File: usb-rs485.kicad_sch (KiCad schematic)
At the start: 0 parts

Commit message: routed, thru holes. ready to order i think
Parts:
- added J2, J3: ~, robot-cortex:ThruHoleBreadboardX4, symbol usb-rs485:ThruHoleX4
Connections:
- net 3V3: now also J3.1
- net GND: now also J2.4, J3.4
- net RX: now also J3.2
- net TX: now also J3.3
- net VUSB: now also J2.1
- new net RS485 Transceiver/RS485-A: J2.2
- new net RS485 Transceiver/RS485-B: J2.3
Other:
- sheet RS485 Transceiver ports: added RS485-A, RS485-B; removed none
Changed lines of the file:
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@@
 (kicad_sch (version 20230121) (generator eeschema)
   (paper "A3")
+  (wire (pts (xy 328.93 173.99) (xy 328.93 174.625))
+    (stroke (width 0) (type default))
+  )
+  (wire (pts (xy 328.93 154.94) (xy 328.93 155.575))
+    (stroke (width 0) (type default))
+  )
   (wire (pts (xy 295.91 144.78) (xy 299.085 144.78))
     (stroke (width 0) (type default))
   )
+  (wire (pts (xy 328.93 166.37) (xy 329.565 166.37))
+    (stroke (width 0) (type default))
+  )
+  (wire (pts (xy 328.93 173.99) (xy 329.565 173.99))
+    (stroke (width 0) (type default))
+  )
+  (wire (pts (xy 328.93 165.735) (xy 328.93 166.37))
+    (stroke (width 0) (type default))
+  )
   (wire (pts (xy 279.4 152.4) (xy 299.085 152.4))
     (stroke (width 0) (type default))
@@
     (stroke (width 0) (type default))
   )
+  (wire (pts (xy 322.58 149.86) (xy 329.565 149.86))
+    (stroke (width 0) (type default))
+  )
+  (wire (pts (xy 328.93 147.32) (xy 329.565 147.32))
+    (stroke (width 0) (type default))
+  )
   (wire (pts (xy 295.91 144.78) (xy 295.91 141.605))
     (stroke (width 0) (type default))
@@
     (stroke (width 0) (type default))
   )
+  (wire (pts (xy 322.58 152.4) (xy 329.565 152.4))
+    (stroke (width 0) (type default))
+  )
   (wire (pts (xy 279.4 149.86) (xy 299.085 149.86))
     (stroke (width 0) (type default))
   )
+  (wire (pts (xy 328.93 168.91) (xy 329.565 168.91))
+    (stroke (width 0) (type default))
+  )
+  (wire (pts (xy 328.93 171.45) (xy 329.565 171.45))
+    (stroke (width 0) (type default))
+  )
   (wire (pts (xy 297.18 157.48) (xy 297.18 158.75))
     (stroke (width 0) (type default))
@@
     (stroke (width 0) (type default))
   )
+  (wire (pts (xy 328.93 146.685) (xy 328.93 147.32))
+    (stroke (width 0) (type default))
+  )
+  (wire (pts (xy 328.93 154.94) (xy 329.565 154.94))
+    (stroke (width 0) (type default))
+  )
   (label "VUSB" (at 254.635 142.875 180) (fields_autoplaced)
+    (effects (font (size 1.27 1.27)) (justify right bottom))
+  )
+  (label "TX" (at 328.93 171.45 180) (fields_autoplaced)
     (effects (font (size 1.27 1.27)) (justify right bottom))
   )
@@
     (effects (font (size 1.27 1.27)) (justify right bottom))
   )
+  (label "RX" (at 328.93 168.91 180) (fields_autoplaced)
+    (effects (font (size 1.27 1.27)) (justify right bottom))
+  )
   (label "3V3" (at 293.37 145.415 180) (fields_autoplaced)
     (effects (font (size 1.27 1.27)) (justify right bottom))
@@
   (label "RX" (at 287.02 149.86 0) (fields_autoplaced)
     (effects (font (size 1.27 1.27)) (justify left bottom))
+  )
+  (label "VUSB" (at 328.93 146.685 180) (fields_autoplaced)
+    (effects (font (size 1.27 1.27)) (justify right bottom))
+  )
+  (label "3V3" (at 328.93 165.735 180) (fields_autoplaced)
+    (effects (font (size 1.27 1.27)) (justify right bottom))
   )
   (symbol (lib_id "power:GND") (at 297.18 158.75 0) (unit 1)
@@
     )
   )
-  (sheet (at 299.085 142.875) (size 12.7 16.51)
+  (symbol (lib_id "power:GND") (at 328.93 155.575 0) (unit 1)
+    (in_bom yes) (on_board yes) (dnp no)
+    (property "Reference" "#PWR011" (at 328.93 161.925 0)
+      (effects (font (size 1.27 1.27)) hide)
+    )
+    (property "Value" "GND" (at 328.93 159.385 0)
+      (effects (font (size 1.27 1.27)))
+    )
+    (property "Footprint" "" (at 328.93 155.575 0)
+      (effects (font (size 1.27 1.27)) hide)
+    )
+    (property "Datasheet" "" (at 328.93 155.575 0)
+      (effects (font (size 1.27 1.27)) hide)
+    )
+    (pin "1")
+    (instances
+      (project "usb-rs485"
+        (path "/19e4cb9f-d0a4-4ce0-8aa4-5fe95563dc37"
+          (reference "#PWR011") (unit 1)
+        )
+      )
+    )
+  )
+  (symbol (lib_id "usb-rs485:ThruHoleX4") (at 332.105 170.18 0) (mirror y) (unit 1)
+    (in_bom no) (on_board yes) (dnp no) (fields_autoplaced)
+    (property "Reference" "J3" (at 336.55 170.18 0)
+      (effects (font (size 1.27 1.27)) (justify right))
+    )
+    (property "Value" "~" (at 330.835 168.91 0)
+      (effects (font (size 1.27 1.27)))
+    )
+    (property "Footprint" "robot-cortex:ThruHoleBreadboardX4" (at 330.835 168.91 0)
+      (effects (font (size 1.27 1.27)) hide)
+    )
+    (property "Datasheet" "" (at 330.835 168.91 0)
+      (effects (font (size 1.27 1.27)) hide)
+    )
+    (pin "3")
+    (pin "4")
+    (pin "2")
+    (pin "1")
+    (instances
+      (project "usb-rs485"
+        (path "/19e4cb9f-d0a4-4ce0-8aa4-5fe95563dc37"
+          (reference "J3") (unit 1)
+        )
+      )
+    )
+  )
+  (symbol (lib_id "usb-rs485:ThruHoleX4") (at 332.105 151.13 0) (mirror y) (unit 1)
+    (in_bom no) (on_board yes) (dnp no) (fields_autoplaced)
+    (property "Reference" "J2" (at 336.55 151.13 0)
+      (effects (font (size 1.27 1.27)) (justify right))
+    )
+    (property "Value" "~" (at 330.835 149.86 0)
+      (effects (font (size 1.27 1.27)))
+    )
+    (property "Footprint" "robot-cortex:ThruHoleBreadboardX4" (at 330.835 149.86 0)
+      (effects (font (size 1.27 1.27)) hide)
+    )
+    (property "Datasheet" "" (at 330.835 149.86 0)
+      (effects (font (size 1.27 1.27)) hide)
+    )
+    (pin "3")
+    (pin "4")
+    (pin "2")
+    (pin "1")
+    (instances
+      (project "usb-rs485"
+        (path "/19e4cb9f-d0a4-4ce0-8aa4-5fe95563dc37"
+          (reference "J2") (unit 1)
+        )
+      )
+    )
+  )
+  (symbol (lib_id "power:GND") (at 328.93 174.625 0) (unit 1)
+    (in_bom yes) (on_board yes) (dnp no)
+    (property "Reference" "#PWR012" (at 328.93 180.975 0)
+      (effects (font (size 1.27 1.27)) hide)
+    )
+    (property "Value" "GND" (at 328.93 178.435 0)
+      (effects (font (size 1.27 1.27)))
+    )
+    (property "Footprint" "" (at 328.93 174.625 0)
+      (effects (font (size 1.27 1.27)) hide)
+    )
+    (property "Datasheet" "" (at 328.93 174.625 0)
+      (effects (font (size 1.27 1.27)) hide)
+    )
+    (pin "1")
+    (instances
+      (project "usb-rs485"
+        (path "/19e4cb9f-d0a4-4ce0-8aa4-5fe95563dc37"
+          (reference "#PWR012") (unit 1)
+        )
+      )
+    )
+  )
+  (sheet (at 299.085 142.875) (size 23.495 16.51)
     (stroke (width 0.1524) (type solid))
     (fill (color 0 0 0 0.0000))
@@
       (effects (font (size 1.27 1.27)) (justify left))
     )
-    (instances
+    (pin "RS485-B" input (at 322.58 152.4 0)
+      (effects (font (size 1.27 1.27)) (justify right))
+    )
+    (pin "RS485-A" input (at 322.58 149.86 0)
+      (effects (font (size 1.27 1.27)) (justify right))
+    )
+    (instances

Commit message: rename library to be for this
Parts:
- J2, J3: footprint robot-cortex:ThruHoleBreadboardX4 -> usb-rs485:ThruHoleBreadboardX4
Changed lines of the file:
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@@
       (effects (font (size 1.27 1.27)))
     )
-    (property "Footprint" "robot-cortex:ThruHoleBreadboardX4" (at 330.835 168.91 0)
+    (property "Footprint" "usb-rs485:ThruHoleBreadboardX4" (at 330.835 168.91 0)
       (effects (font (size 1.27 1.27)) hide)
     )
@@
       (effects (font (size 1.27 1.27)))
     )
-    (property "Footprint" "robot-cortex:ThruHoleBreadboardX4" (at 330.835 149.86 0)
+    (property "Footprint" "usb-rs485:ThruHoleBreadboardX4" (at 330.835 149.86 0)
       (effects (font (size 1.27 1.27)) hide)
     )

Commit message: starting to add power
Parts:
- added R4: 470k, usb-rs485:R_0402_1005Metric, symbol usb-rs485:Resistor
- added R5: 150k, usb-rs485:R_0402_1005Metric, symbol usb-rs485:Resistor
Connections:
- new net PSU_TPS63070RNMR/FB: R4.2, R5.1
- new net PSU_TPS63070RNMR/FB_GND: R5.2
- new net PSU_TPS63070RNMR/FB_VOUT: R4.1
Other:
- added sheet PSU_TPS63070RNMR (PSU_TPS63070RNMR.kicad_sch)
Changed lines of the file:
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@@
 (kicad_sch (version 20230121) (generator eeschema)
   (paper "A3")
+  (junction (at 302.26 202.565) (diameter 0) (color 0 0 0 0)
+  )
+  (junction (at 285.115 180.975) (diameter 0) (color 0 0 0 0)
+  )
   (wire (pts (xy 328.93 173.99) (xy 328.93 174.625))
     (stroke (width 0) (type default))
   )
+  (wire (pts (xy 285.115 178.435) (xy 285.115 180.975))
+    (stroke (width 0) (type default))
+  )
   (wire (pts (xy 328.93 154.94) (xy 328.93 155.575))
     (stroke (width 0) (type default))
   )
+  (wire (pts (xy 302.26 202.565) (xy 300.355 202.565))
+    (stroke (width 0) (type default))
+  )
+  (wire (pts (xy 300.355 181.61) (xy 301.625 181.61))
+    (stroke (width 0) (type default))
+  )
   (wire (pts (xy 295.91 144.78) (xy 299.085 144.78))
     (stroke (width 0) (type default))
@@
     (stroke (width 0) (type default))
   )
+  (wire (pts (xy 302.26 213.995) (xy 300.355 213.995))
+    (stroke (width 0) (type default))
+  )
   (wire (pts (xy 279.4 152.4) (xy 299.085 152.4))
     (stroke (width 0) (type default))
@@
     (stroke (width 0) (type default))
   )
+  (wire (pts (xy 302.26 192.405) (xy 302.26 193.04))
+    (stroke (width 0) (type default))
+  )
   (wire (pts (xy 328.93 147.32) (xy 329.565 147.32))
     (stroke (width 0) (type default))
   )
+  (wire (pts (xy 285.115 186.69) (xy 285.115 186.055))
+    (stroke (width 0) (type default))
+  )
   (wire (pts (xy 295.91 144.78) (xy 295.91 141.605))
     (stroke (width 0) (type default))
@@
     (stroke (width 0) (type default))
   )
+  (wire (pts (xy 300.355 192.405) (xy 302.26 192.405))
+    (stroke (width 0) (type default))
+  )
   (wire (pts (xy 257.81 142.875) (xy 254.635 142.875))
     (stroke (width 0) (type default))
@@
     (stroke (width 0) (type default))
   )
+  (wire (pts (xy 302.26 212.09) (xy 302.26 213.995))
+    (stroke (width 0) (type default))
+  )
   (wire (pts (xy 297.18 157.48) (xy 297.18 158.75))
     (stroke (width 0) (type default))
@@
     (stroke (width 0) (type default))
   )
+  (wire (pts (xy 283.21 178.435) (xy 285.115 178.435))
+    (stroke (width 0) (type default))
+  )
   (wire (pts (xy 254.635 160.655) (xy 254.635 163.195))
     (stroke (width 0) (type default))
   )
+  (wire (pts (xy 285.115 180.975) (xy 287.02 180.975))
+    (stroke (width 0) (type default))
+  )
   (wire (pts (xy 257.81 160.655) (xy 254.635 160.655))
     (stroke (width 0) (type default))
   )
+  (wire (pts (xy 302.26 200.66) (xy 302.26 202.565))
+    (stroke (width 0) (type default))
+  )
+  (wire (pts (xy 302.26 202.565) (xy 302.26 204.47))
+    (stroke (width 0) (type default))
+  )
   (wire (pts (xy 293.37 147.32) (xy 293.37 145.415))
     (stroke (width 0) (type default))
   )
+  (wire (pts (xy 285.115 186.055) (xy 287.02 186.055))
+    (stroke (width 0) (type default))
+  )
   (wire (pts (xy 328.93 146.685) (xy 328.93 147.32))
     (stroke (width 0) (type default))
@@
     (stroke (width 0) (type default))
   )
+  (wire (pts (xy 282.575 180.975) (xy 285.115 180.975))
+    (stroke (width 0) (type default))
+  )
+  (label "V_GATEDRIVE" (at 283.21 178.435 180) (fields_autoplaced)
+    (effects (font (size 1.27 1.27)) (justify right bottom))
+  )
   (label "VUSB" (at 254.635 142.875 180) (fields_autoplaced)
     (effects (font (size 1.27 1.27)) (justify right bottom))
   )
   (label "TX" (at 328.93 171.45 180) (fields_autoplaced)
+    (effects (font (size 1.27 1.27)) (justify right bottom))
+  )
+  (label "V_LOGIC" (at 282.575 180.975 180) (fields_autoplaced)
     (effects (font (size 1.27 1.27)) (justify right bottom))
   )
@@
         (path "/19e4cb9f-d0a4-4ce0-8aa4-5fe95563dc37"
           (reference "#PWR073") (unit 1)
+        )
+      )
+    )
+  )
+  (symbol (lib_id "power:GND") (at 285.115 186.69 0) (mirror y) (unit 1)
+    (in_bom yes) (on_board yes) (dnp no) (fields_autoplaced)
+    (property "Reference" "#PWR013" (at 285.115 193.04 0)
+      (effects (font (size 1.27 1.27)) hide)
+    )
+    (property "Value" "GND" (at 285.115 191.77 0)
+      (effects (font (size 1.27 1.27)))
+    )
+    (property "Footprint" "" (at 285.115 186.69 0)
+      (effects (font (size 1.27 1.27)) hide)
+    )
+    (property "Datasheet" "" (at 285.115 186.69 0)
+      (effects (font (size 1.27 1.27)) hide)
+    )
+    (pin "1")
+    (instances
+      (project "usb-rs485"
+        (path "/19e4cb9f-d0a4-4ce0-8aa4-5fe95563dc37"
+          (reference "#PWR013") (unit 1)
+        )
+      )
+    )
+  )
+  (symbol (lib_id "usb-rs485:Resistor") (at 302.26 196.85 0) (unit 1)
+    (in_bom yes) (on_board yes) (dnp no)
+    (property "Reference" "R4" (at 303.53 197.485 0)
+      (effects (font (size 1.27 1.27)) (justify left))
+    )
+    (property "Value" "470k" (at 306.07 199.39 0)
+      (effects (font (size 1.27 1.27)))
+    )
+    (property "Footprint" "usb-rs485:R_0402_1005Metric" (at 297.18 184.15 0)
+      (effects (font (size 1.27 1.27)) hide)
+    )
+    (property "Datasheet" "~" (at 302.26 196.85 0)
+      (effects (font (size 1.27 1.27)) hide)
+    )
+    (pin "1")
+    (pin "2")
+    (instances
+      (project "usb-rs485"
+        (path "/19e4cb9f-d0a4-4ce0-8aa4-5fe95563dc37"
+          (reference "R4") (unit 1)
         )
       )
@@
       )
     )
+  )
+  (symbol (lib_id "power:+3V3") (at 301.625 181.61 0) (mirror y) (unit 1)
+    (in_bom yes) (on_board yes) (dnp no)
+    (property "Reference" "#PWR014" (at 301.625 185.42 0)
+      (effects (font (size 1.27 1.27)) hide)
+    )
+    (property "Value" "+3V3" (at 305.435 180.34 0)
+      (effects (font (size 1.27 1.27)))
+    )
+    (property "Footprint" "" (at 301.625 181.61 0)
+      (effects (font (size 1.27 1.27)) hide)
+    )
+    (property "Datasheet" "" (at 301.625 181.61 0)
+      (effects (font (size 1.27 1.27)) hide)
+    )
+    (pin "1")
+    (instances
+      (project "usb-rs485"
+        (path "/19e4cb9f-d0a4-4ce0-8aa4-5fe95563dc37"
+          (reference "#PWR014") (unit 1)
+        )
+      )
+    )
+  )
+  (symbol (lib_id "usb-rs485:Resistor") (at 302.26 208.28 0) (unit 1)
+    (in_bom yes) (on_board yes) (dnp no)
+    (property "Reference" "R5" (at 303.53 208.915 0)
+      (effects (font (size 1.27 1.27)) (justify left))
+    )
+    (property "Value" "150k" (at 306.07 210.82 0)
+      (effects (font (size 1.27 1.27)))
+    )
+    (property "Footprint" "usb-rs485:R_0402_1005Metric" (at 297.18 195.58 0)
+      (effects (font (size 1.27 1.27)) hide)
+    )
+    (property "Datasheet" "~" (at 302.26 208.28 0)
+      (effects (font (size 1.27 1.27)) hide)
+    )
+    (pin "1")
+    (pin "2")
+    (instances
+      (project "usb-rs485"
+        (path "/19e4cb9f-d0a4-4ce0-8aa4-5fe95563dc37"
+          (reference "R5") (unit 1)
+        )
+      )
+    )
+  )
+  (sheet (at 287.02 179.705) (size 13.335 35.56)
+    (stroke (width 0.1524) (type solid))
+    (fill (color 0 0 0 0.0000))
+    (property "Sheetname" "PSU_TPS63070RNMR" (at 286.385 177.8 0)
+      (effects (font (size 1.27 1.27)) (justify left bottom))
+    )
+    (property "Sheetfile" "PSU_TPS63070RNMR.kicad_sch" (at 287.02 216.535 0)
+      (effects (font (size 1.27 1.27)) (justify left top))
+    )
+    (pin "VOUT" input (at 300.355 181.61 0)
+      (effects (font (size 1.27 1.27)) (justify right))
+    )
+    (pin "GND" input (at 287.02 186.055 180)
+      (effects (font (size 1.27 1.27)) (justify left))
+    )
+    (pin "VIN" input (at 287.02 180.975 180)
+      (effects (font (size 1.27 1.27)) (justify left))
+    )
+    (pin "FB_VOUT" input (at 300.355 192.405 0)
+      (effects (font (size 1.27 1.27)) (justify right))
+    )
+    (pin "FB" input (at 300.355 202.565 0)
+      (effects (font (size 1.27 1.27)) (justify right))
+    )
+    (pin "FB_GND" input (at 300.355 213.995 0)
+      (effects (font (size 1.27 1.27)) (justify right))
+    )
+    (instances
+      (project "foc-pcb"
+        (path "/2b52ab19-a93e-4439-8602-a1380e4825c0" (page "5"))
+      )
+      (project "usb-rs485"
+        (path "/19e4cb9f-d0a4-4ce0-8aa4-5fe95563dc37" (page "3"))
+      )
+    )

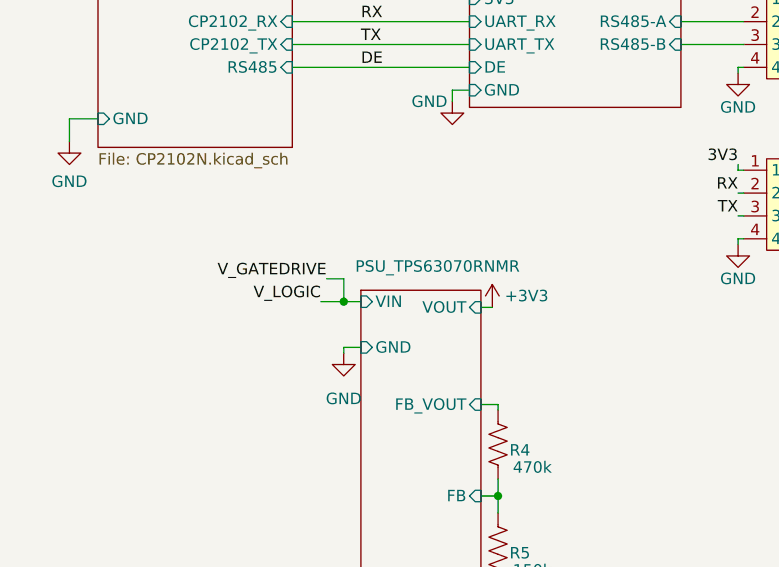
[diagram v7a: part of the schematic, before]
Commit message: wiring in boost to 6V
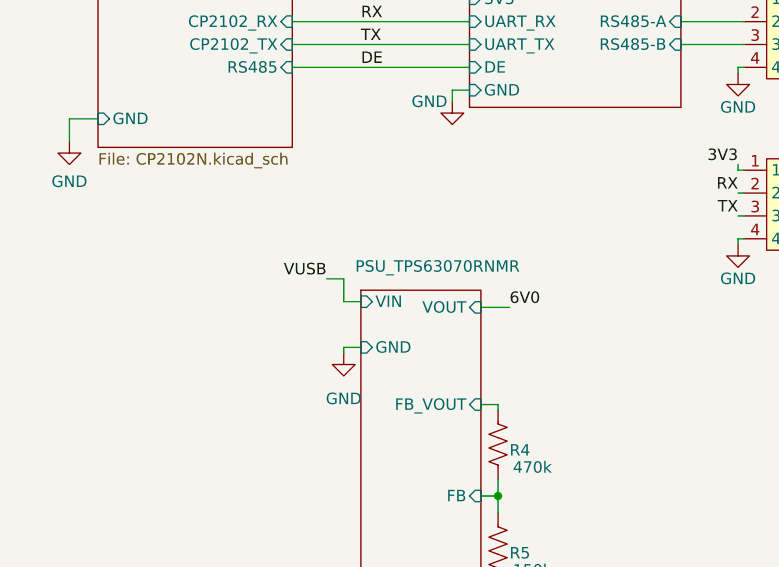
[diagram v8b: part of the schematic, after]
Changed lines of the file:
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@@
   (junction (at 302.26 202.565) (diameter 0) (color 0 0 0 0)
   )
-  (junction (at 285.115 180.975) (diameter 0) (color 0 0 0 0)
-  )
   (wire (pts (xy 328.93 173.99) (xy 328.93 174.625))
     (stroke (width 0) (type default))
@@
     (stroke (width 0) (type default))
   )
-  (wire (pts (xy 300.355 181.61) (xy 301.625 181.61))
+  (wire (pts (xy 300.355 181.61) (xy 303.53 181.61))
     (stroke (width 0) (type default))
   )
@@
     (stroke (width 0) (type default))
   )
-  (wire (pts (xy 282.575 180.975) (xy 285.115 180.975))
-    (stroke (width 0) (type default))
-  )
-  (label "V_GATEDRIVE" (at 283.21 178.435 180) (fields_autoplaced)
-    (effects (font (size 1.27 1.27)) (justify right bottom))
+  (label "6V0" (at 303.53 181.61 0) (fields_autoplaced)
+    (effects (font (size 1.27 1.27)) (justify left bottom))
   )
   (label "VUSB" (at 254.635 142.875 180) (fields_autoplaced)
@@
   )
   (label "TX" (at 328.93 171.45 180) (fields_autoplaced)
-    (effects (font (size 1.27 1.27)) (justify right bottom))
-  )
-  (label "V_LOGIC" (at 282.575 180.975 180) (fields_autoplaced)
     (effects (font (size 1.27 1.27)) (justify right bottom))
   )
@@
   (label "TX" (at 287.02 152.4 0) (fields_autoplaced)
     (effects (font (size 1.27 1.27)) (justify left bottom))
+  )
+  (label "VUSB" (at 283.21 178.435 180) (fields_autoplaced)
+    (effects (font (size 1.27 1.27)) (justify right bottom))
   )
   (label "DE" (at 287.02 154.94 0) (fields_autoplaced)
@@
         )
       )
-    )
-  )
-  (symbol (lib_id "power:+3V3") (at 301.625 181.61 0) (mirror y) (unit 1)
-    (in_bom yes) (on_board yes) (dnp no)
-    (property "Reference" "#PWR014" (at 301.625 185.42 0)
-      (effects (font (size 1.27 1.27)) hide)
-    )
-    (property "Value" "+3V3" (at 305.435 180.34 0)
-      (effects (font (size 1.27 1.27)))
-    )
-    (property "Footprint" "" (at 301.625 181.61 0)
-      (effects (font (size 1.27 1.27)) hide)
-    )
-    (property "Datasheet" "" (at 301.625 181.61 0)
-      (effects (font (size 1.27 1.27)) hide)
-    )
-    (pin "1")
-    (instances
-      (project "usb-rs485"
-        (path "/19e4cb9f-d0a4-4ce0-8aa4-5fe95563dc37"
-          (reference "#PWR014") (unit 1)
-        )
-      )
